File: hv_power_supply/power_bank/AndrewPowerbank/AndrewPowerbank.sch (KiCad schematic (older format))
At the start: 43 parts, among them J1 Conn_01x02, J2 Conn_01x02, J3 USB-A-S-X-X-SM2, J4 USB-Micro-1981568-1, Q1 SSM3K333R, U2 MCP73871T-2CCI_ML, U3 TPS61090RSAR

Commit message: Initial Commit
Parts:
- removed J1, J2: Conn_01x02, symbol Connector_Generic:Conn_01x02
- added J1, J2: CONN_01x02, Connector_PinHeader_2.54mm:PinHeader_1x02_P2.54mm_Vertical, symbol formula:CONN_01x02
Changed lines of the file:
@@
 Micro USB Input
-$Comp
-L Connector_Generic:Conn_01x02 J1
-U 1 1 5FD375C1
-P 1300 5600
-F 0 "J1" H 1218 5275 50  0000 C CNN
-F 1 "Conn_01x02" H 1218 5366 50  0000 C CNN
-F 2 "" H 1300 5600 50  0001 C CNN
-F 3 "~" H 1300 5600 50  0001 C CNN
-	1    1300 5600
-	-1   0    0    1
-$EndComp
 $Comp
 L formula:1.5A_Fuse F1
@@
 Text Notes 1250 5150 0    50   ~ 0
 Battery
-$Comp
-L Connector_Generic:Conn_01x02 J2
-U 1 1 5FD3CA00
-P 1300 4700
-F 0 "J2" H 1218 4375 50  0000 C CNN
-F 1 "Conn_01x02" H 1218 4466 50  0000 C CNN
-F 2 "" H 1300 4700 50  0001 C CNN
-F 3 "~" H 1300 4700 50  0001 C CNN
-	1    1300 4700
-	-1   0    0    1
-$EndComp
 $Comp
 L power:GND #PWR01
@@
 	1    0    0    -1
 $EndComp
-Connection ~ 2050 3150
-Wire Wire Line
-	2050 3150 2550 3150
-Wire Wire Line
-	1850 3150 2050 3150
 $Comp
 L power:GND #PWR08
@@
 Wire Wire Line
 	2550 2950 2550 3150
-Connection ~ 2550 3150
 $Comp
 L formula:R_43k R3
@@
 Text Notes 7100 3800 2    50   ~ 0
 connect gndpwr to gnd @ fb pin gnd
+$Comp
+L formula:CONN_01x02 J2
+U 1 1 5FCC75FF
+P 1300 4700
+F 0 "J2" H 1218 4375 50  0000 C CNN
+F 1 "CONN_01x02" H 1218 4466 50  0000 C CNN
+F 2 "Connector_PinHeader_2.54mm:PinHeader_1x02_P2.54mm_Vertical" H 1200 4700 50  0001 C CNN
+F 3 "https://katalog.we-online.de/em/datasheet/6130xx11121.pdf" H 1300 4800 50  0001 C CNN
+F 4 "DK" H 1400 4900 50  0001 C CNN "MFN"
+F 5 "732-5315-ND" H 1500 5000 50  0001 C CNN "MPN"
+	1    1300 4700
+	-1   0    0    1
+$EndComp
+$Comp
+L formula:CONN_01x02 J1
+U 1 1 5FCC9A30
+P 1300 5600
+F 0 "J1" H 1218 5275 50  0000 C CNN
+F 1 "CONN_01x02" H 1218 5366 50  0000 C CNN
+F 2 "Connector_PinHeader_2.54mm:PinHeader_1x02_P2.54mm_Vertical" H 1200 5600 50  0001 C CNN
+F 3 "https://katalog.we-online.de/em/datasheet/6130xx11121.pdf" H 1300 5700 50  0001 C CNN
+F 4 "DK" H 1400 5800 50  0001 C CNN "MFN"
+F 5 "732-5315-ND" H 1500 5900 50  0001 C CNN "MPN"
+	1    1300 5600
+	-1   0    0    1
+$EndComp
+Wire Wire Line
+	2550 3150 2050 3150
+Connection ~ 2550 3150
+Wire Wire Line
+	2050 3150 1850 3150
+Connection ~ 1850 7200
 $EndSCHEMATC

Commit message: Fixed issues regarding R15, R16 connections, acute trace connections. Added via pathways. \ R15 is now a 1M pull-up resistor connected to VOUT lines on U3 component after C6, C7 components, before R18. Former +BATT connection to R16 is now +5V. Added vias & pathways connecting +5V, VBUS, BATT+, GND nets.
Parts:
- removed R15: R_10K, footprints:R_0805_OEM, symbol formula:R_10K
- added R15: R_1M, footprints:R_0805_OEM, symbol formula:R_1M
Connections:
- net labels removed: +BATT
- wire segments 95 -> 98
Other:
- moved on the sheet: D3, D4, Q1, R12, R16, R18, TP1

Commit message: 1st Rev of Andrew's Personal Onboarding Project
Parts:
- removed C5: C_10nF, footprints:C_0805_OEM, symbol formula:C_10nF
- added C3, C5, C7: C_4.7uF, footprints:C_0603_1608Metric, symbol formula:C_4.7uF
- added C8: C_10pF, footprints:C_0603_1608Metric, symbol formula:C_18pF
- renumbered C7 to C10, C3 to C6, C6 to C9, D2 to D1, D1 to D2, J2 to J1, J1 to J2, R13 to R11, R17 to R12, R14 to R13, R11 to R14, R12 to R15, R15 to R17, R7 to R5, R8 to R6, R5 to R7, R6 to R8, TP2 to TP1, TP5 to TP2, TP1 to TP5, U2 to U1, U3 to U2
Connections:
- net +5V: now also C8.1
- net +BATT: now also C7.2; no longer R11.1, U1.1 (OUT), U1.20 (OUT)
- net Battery+: now also C3.1
- net GND: now also C3.2; no longer U1.10 (VSS), U1.21 (EP)
- net VBUS: now also R11.1, C5.1; no longer U1.18 (IN), U1.19 (IN)
- net at R14.2, R15.2, U2.14 (FB): now also C8.2
- new net: C7.1, U1.1 (OUT)
- new net: U1.10 (VSS), U1.21 (EP)
- new net: C5.2, U1.18 (IN), U1.19 (IN)
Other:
- moved on the sheet: C9, D1, R11, R14, R15, TP2

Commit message: Revamp first-year onboarding project board after feedback.
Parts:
- removed J1, J2: CONN_01x02, Connector_PinHeader_2.54mm:PinHeader_1x02_P2.54mm_Vertical, symbol formula:CONN_01x02
- added J1, J2, J5: NanoFit_RA_TH_02, footprints:NanoFit_Molex_1x02x2.50mm_Angled_OEM, symbol formula:NanoFit_RA_TH_02
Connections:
- net 16KThermistor: now also J1.2
- net GND: now also J1.1, J2.1
- net at F1.1: now also J2.2
- net at C7.1, U1.1 (OUT): now also U1.20 (OUT)
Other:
- note added: "Switch"
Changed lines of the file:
@@
 L power:GND #PWR02
 U 1 1 5FD3A846
-P 1500 5600
-F 0 "#PWR02" H 1500 5350 50  0001 C CNN
-F 1 "GND" H 1505 5427 50  0000 C CNN
-F 2 "" H 1500 5600 50  0001 C CNN
-F 3 "" H 1500 5600 50  0001 C CNN
-	1    1500 5600
+P 1500 5650
+F 0 "#PWR02" H 1500 5400 50  0001 C CNN
+F 1 "GND" H 1505 5477 50  0000 C CNN
+F 2 "" H 1500 5650 50  0001 C CNN
+F 3 "" H 1500 5650 50  0001 C CNN
+	1    1500 5650
 	1    0    0    -1
 $EndComp
@@
 L power:GND #PWR01
 U 1 1 5FD416C2
-P 1500 4700
-F 0 "#PWR01" H 1500 4450 50  0001 C CNN
-F 1 "GND" H 1505 4527 50  0000 C CNN
-F 2 "" H 1500 4700 50  0001 C CNN
-F 3 "" H 1500 4700 50  0001 C CNN
-	1    1500 4700
-	1    0    0    -1
-$EndComp
-Text Label 1500 4600 0    50   ~ 0
+P 1500 4800
+F 0 "#PWR01" H 1500 4550 50  0001 C CNN
+F 1 "GND" H 1505 4627 50  0000 C CNN
+F 2 "" H 1500 4800 50  0001 C CNN
+F 3 "" H 1500 4800 50  0001 C CNN
+	1    1500 4800
+	1    0    0    -1
+$EndComp
+Text Label 1500 4650 0    50   ~ 0
 16KThermistor
-Text Notes 1200 4300 0    50   ~ 0
+Text Notes 1150 4300 0    50   ~ 0
 Thermistor
 $Comp
@@
 Text Notes 7100 3800 2    50   ~ 0
 connect gndpwr to gnd @ fb pin gnd
-$Comp
-L formula:CONN_01x02 J1
-U 1 1 5FCC75FF
-P 1300 4700
-F 0 "J1" H 1218 4375 50  0000 C CNN
-F 1 "CONN_01x02" H 1218 4466 50  0000 C CNN
-F 2 "Connector_PinHeader_2.54mm:PinHeader_1x02_P2.54mm_Vertical" H 1200 4700 50  0001 C CNN
-F 3 "https://katalog.we-online.de/em/datasheet/6130xx11121.pdf" H 1300 4800 50  0001 C CNN
-F 4 "DK" H 1400 4900 50  0001 C CNN "MFN"
-F 5 "732-5315-ND" H 1500 5000 50  0001 C CNN "MPN"
-	1    1300 4700
-	-1   0    0    1
-$EndComp
-$Comp
-L formula:CONN_01x02 J2
-U 1 1 5FCC9A30
-P 1300 5600
-F 0 "J2" H 1218 5275 50  0000 C CNN
-F 1 "CONN_01x02" H 1218 5366 50  0000 C CNN
-F 2 "Connector_PinHeader_2.54mm:PinHeader_1x02_P2.54mm_Vertical" H 1200 5600 50  0001 C CNN
-F 3 "https://katalog.we-online.de/em/datasheet/6130xx11121.pdf" H 1300 5700 50  0001 C CNN
-F 4 "DK" H 1400 5800 50  0001 C CNN "MFN"
-F 5 "732-5315-ND" H 1500 5900 50  0001 C CNN "MPN"
-	1    1300 5600
-	-1   0    0    1
-$EndComp
 Wire Wire Line
 	2550 3150 2050 3150
@@
 	4150 6950 4150 6850
 Connection ~ 4150 6850
+$Comp
+L formula:NanoFit_RA_TH_02 J2
+U 1 1 605E598D
+P 1050 5600
+F 0 "J2" H 942 5213 60  0000 C CNN
+F 1 "NanoFit_RA_TH_02" H 942 5319 60  0000 C CNN
+F 2 "footprints:NanoFit_Molex_1x02x2.50mm_Angled_OEM" H 1050 5000 60  0001 C CNN
+F 3 "https://www.molex.com/pdm_docs/sd/1053131102_sd.pdf" H 1050 5150 60  0001 C CNN
+F 4 "DK" H 1050 6150 50  0001 C CNN "MFN"
+F 5 "WM14972-ND" H 1050 6050 50  0001 C CNN "MPN"
+F 6 "https://www.digikey.com/products/en/connectors-interconnects/rectangular-connectors-headers-male-pins/314?k=nanofit+2&k=&pkeyword=nanofit+2&pv88=2&pv69=367&sf=0&FV=ffe0013a&quantity=&ColumnSort=0&page=1&pageSize=25" H 1050 4800 50  0001 C CNN "PurchasingLink"
+	1    1050 5600
+	-1   0    0    1
+$EndComp
+$Comp
+L formula:NanoFit_RA_TH_02 J1
+U 1 1 605ED628
+P 1050 4750
+F 0 "J1" H 942 4363 60  0000 C CNN
+F 1 "NanoFit_RA_TH_02" H 942 4469 60  0000 C CNN
+F 2 "footprints:NanoFit_Molex_1x02x2.50mm_Angled_OEM" H 1050 4150 60  0001 C CNN
+F 3 "https://www.molex.com/pdm_docs/sd/1053131102_sd.pdf" H 1050 4300 60  0001 C CNN
+F 4 "DK" H 1050 5300 50  0001 C CNN "MFN"
+F 5 "WM14972-ND" H 1050 5200 50  0001 C CNN "MPN"
+F 6 "https://www.digikey.com/products/en/connectors-interconnects/rectangular-connectors-headers-male-pins/314?k=nanofit+2&k=&pkeyword=nanofit+2&pv88=2&pv69=367&sf=0&FV=ffe0013a&quantity=&ColumnSort=0&page=1&pageSize=25" H 1050 3950 50  0001 C CNN "PurchasingLink"
+	1    1050 4750
+	-1   0    0    1
+$EndComp
+$Comp
+L formula:NanoFit_RA_TH_02 J5
+U 1 1 605F0515
+P 2800 4800
+F 0 "J5" H 2692 4413 60  0000 C CNN
+F 1 "NanoFit_RA_TH_02" H 2692 4519 60  0000 C CNN
+F 2 "footprints:NanoFit_Molex_1x02x2.50mm_Angled_OEM" H 2800 4200 60  0001 C CNN
+F 3 "https://www.molex.com/pdm_docs/sd/1053131102_sd.pdf" H 2800 4350 60  0001 C CNN
+F 4 "DK" H 2800 5350 50  0001 C CNN "MFN"
+F 5 "WM14972-ND" H 2800 5250 50  0001 C CNN "MPN"
+F 6 "https://www.digikey.com/products/en/connectors-interconnects/rectangular-connectors-headers-male-pins/314?k=nanofit+2&k=&pkeyword=nanofit+2&pv88=2&pv69=367&sf=0&FV=ffe0013a&quantity=&ColumnSort=0&page=1&pageSize=25" H 2800 4000 50  0001 C CNN "PurchasingLink"
+	1    2800 4800
+	-1   0    0    1
+$EndComp
+Text Notes 2500 4300 0    50   ~ 0
+Switch
+Wire Wire Line
+	5750 5950 5750 5850
+Connection ~ 5750 5850
 $EndSCHEMATC

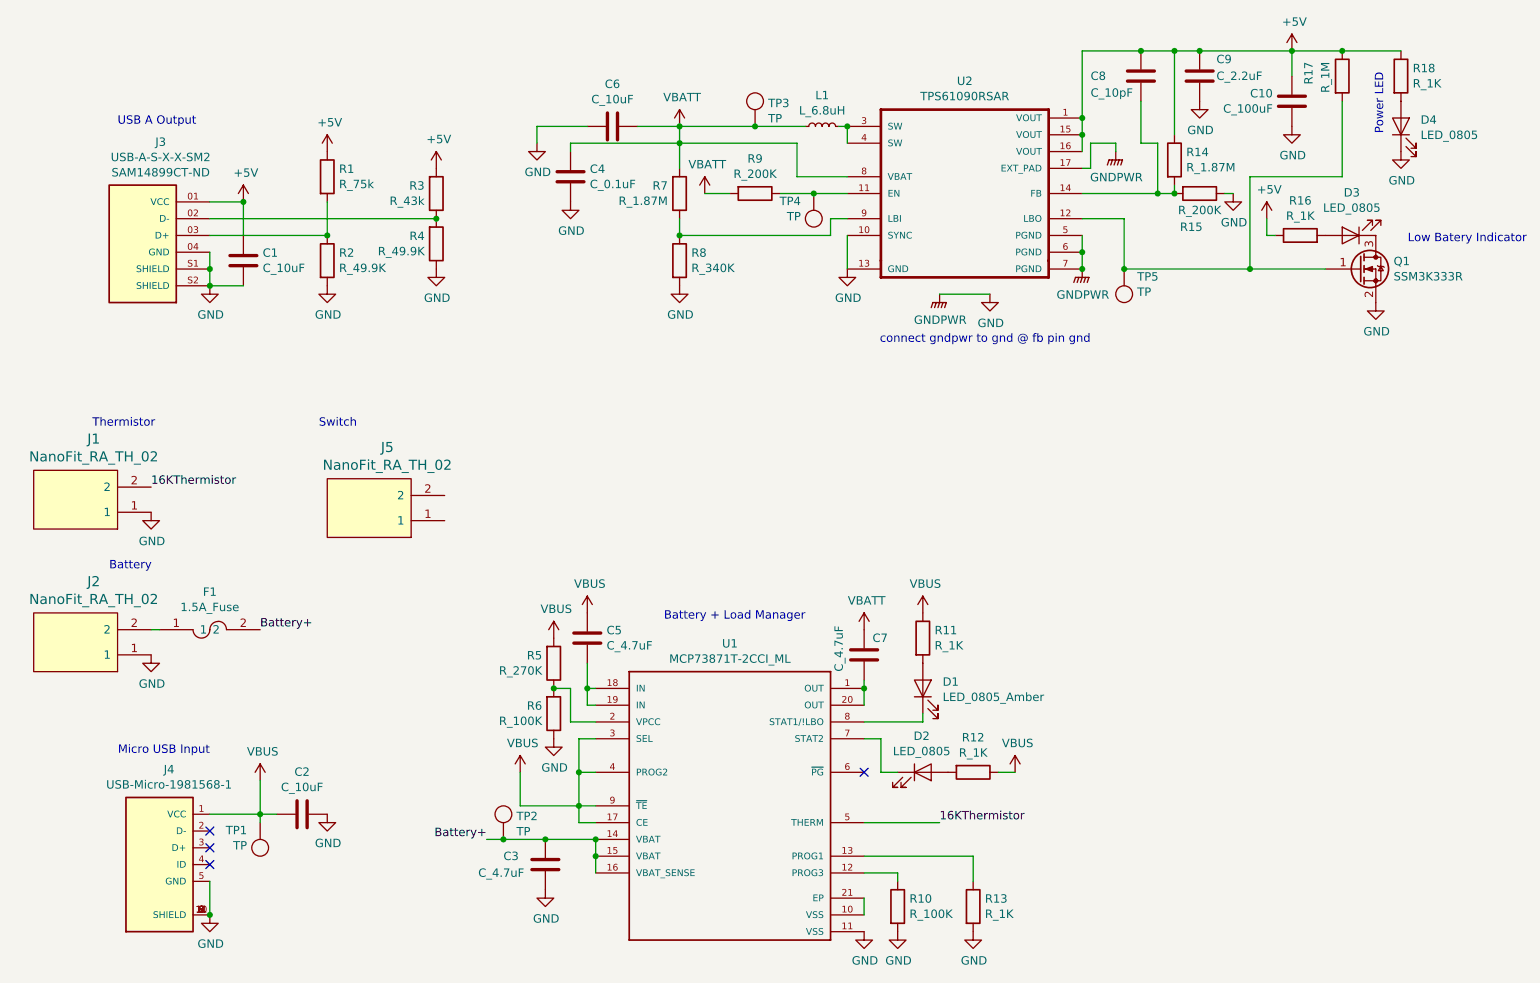
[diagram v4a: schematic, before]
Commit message: Add switch connections, labels to LEDs, name / date.
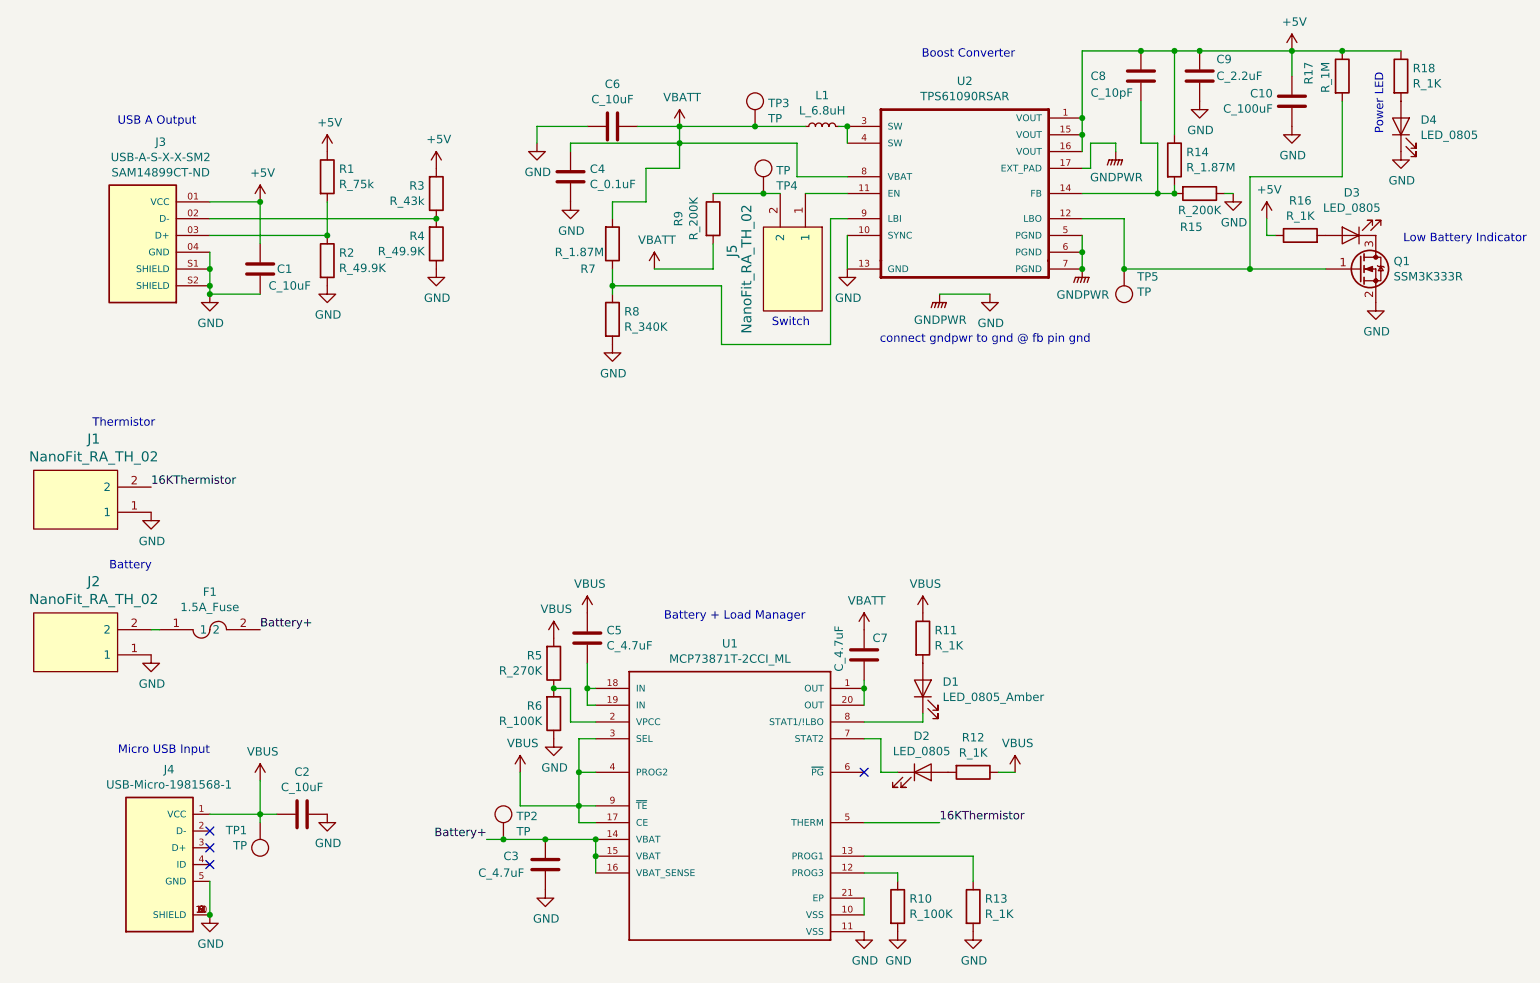
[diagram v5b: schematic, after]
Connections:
- net +5V: no longer J3.03 (D+), R1.2, R2.1
- net at R9.1, TP4.1 (TP): now also J5.2; no longer U2.11 (EN)
- net at J5.1: now also U2.11 (EN)
- new net: J3.03 (D+), R1.2, R2.1
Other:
- note added: "Boost Converter"
- note added: "Low Battery Indicator"
- note removed: "Low Batery Indicator"
- moved on the sheet: C1, J5, R7, R8, R9, TP4

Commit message: Fix issues with board after feedback from Corey.
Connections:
- net GND: now also C5.2
- net VBUS: now also U1.18 (IN), U1.19 (IN)
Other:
- moved on the sheet: C5, R5, R6

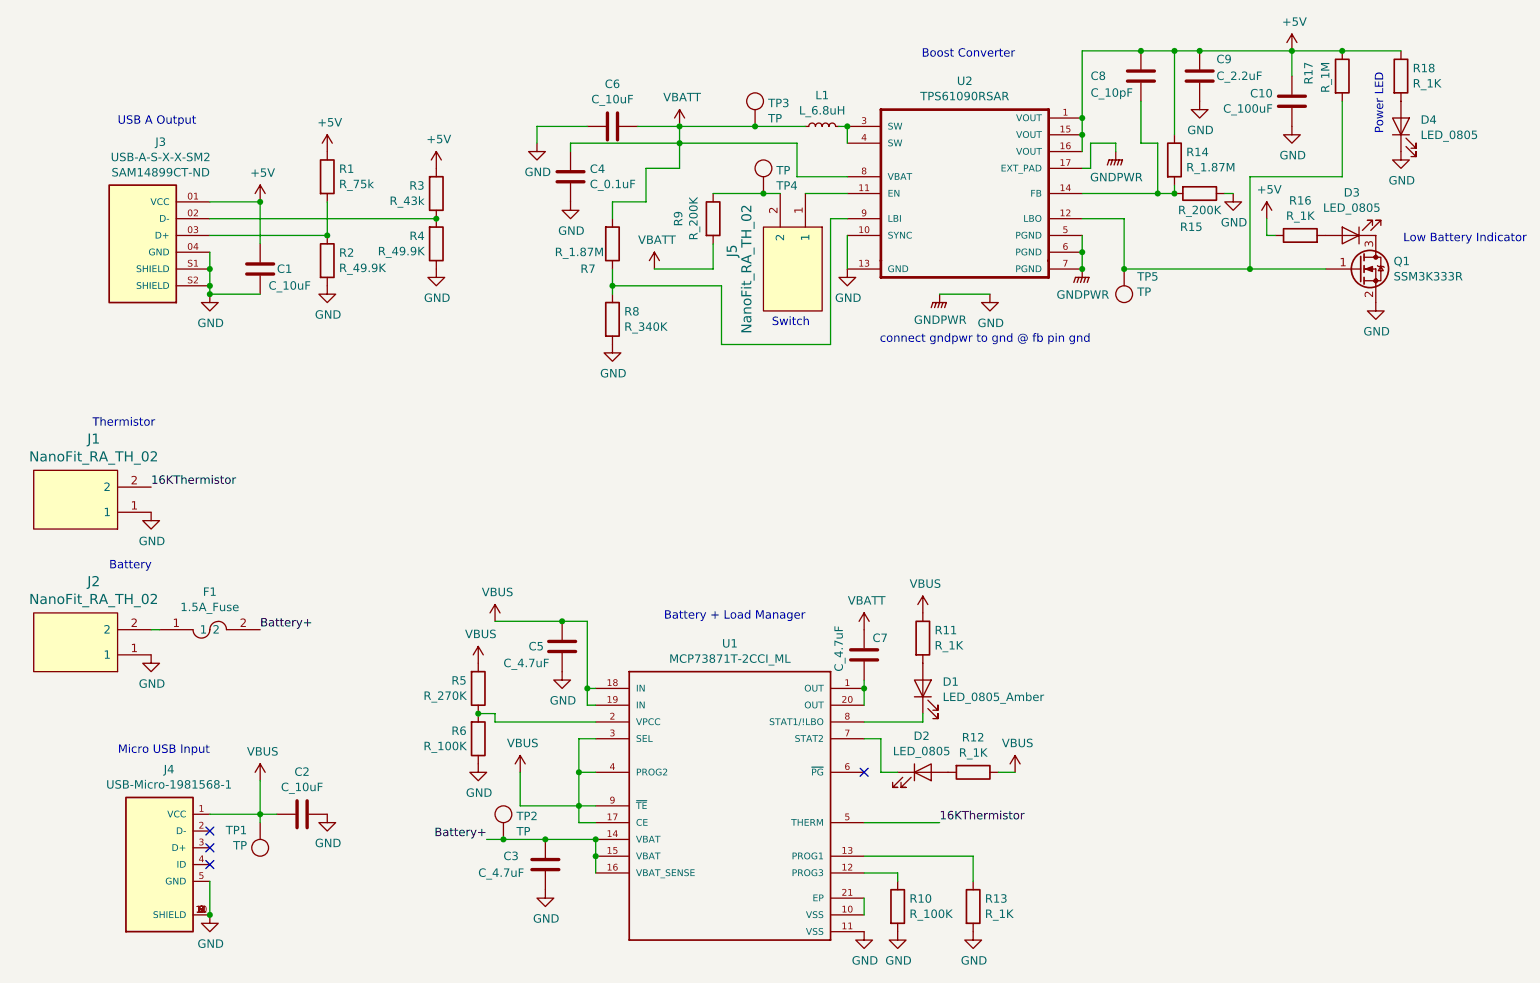
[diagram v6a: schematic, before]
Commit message: Optimize board addressing Wesley's critiques.
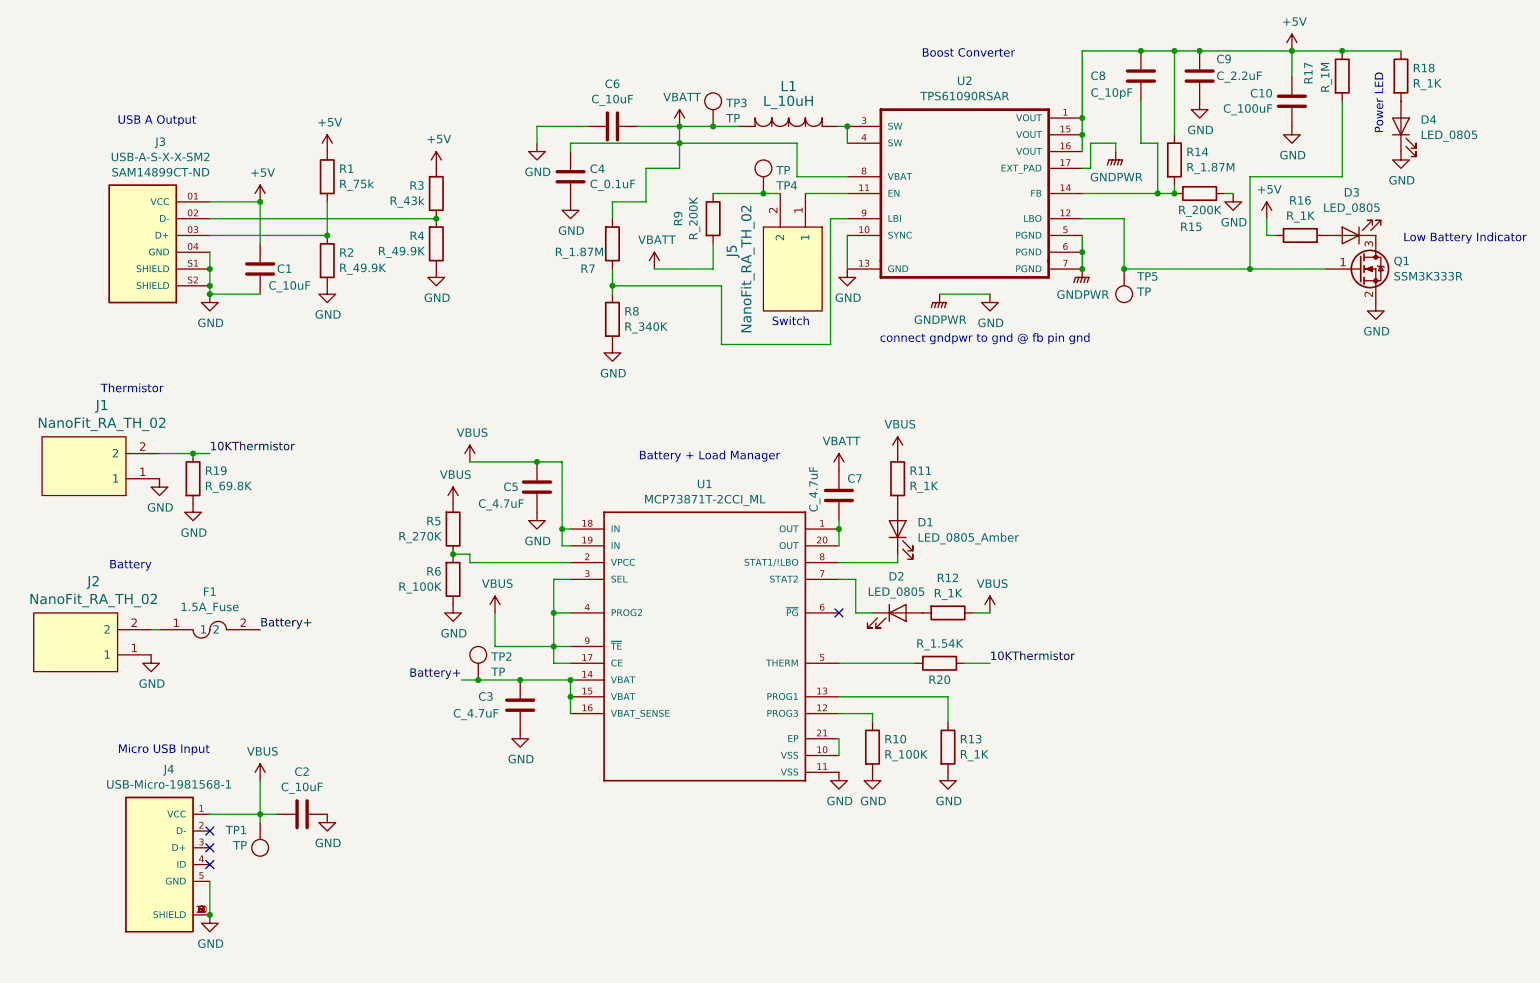
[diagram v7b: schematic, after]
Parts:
- removed L1: L_6.8uH, footprints:L_100uH_OEM, symbol formula:L_6.8uH
- added L1: L_10uH, footprints:BournsInductor, symbol formula:L_10uH
- added R19: R_69.8K, footprints:R_0805_OEM, symbol formula:R_69.8K
- added R20: R_1.54K, footprints:R_0805_OEM, symbol formula:R_1.54K
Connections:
- net +BATT: now also L1.2
- net GND: now also R19.2
- net at U2.3 (SW), U2.4 (SW): now also L1.1
- net 16KThermistor: no longer names the net of U1.5 (THERM)
- net 16KThermistor: now also R20.2; no longer J1.2
- new net 10KThermistor: J1.2, R19.1, R20.1
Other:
- moved on the sheet: C3, C5, C7, D1, D2, J1, R10, R11, R12, R13, R5, R6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
